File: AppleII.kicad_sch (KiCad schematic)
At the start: 0 parts

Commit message: finish tracing
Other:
- sheet Address Decoder and Onboard IO ports: added KBD_Data[0..6]; removed none
- sheet CPU Tranceiver Driver and Data MUX ports: added KBD_Data[0..6]; removed none
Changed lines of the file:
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@@
   (junction (at 140.97 101.6) (diameter 0) (color 0 0 0 0)
+  )
+  (bus (pts (xy 74.93 38.1) (xy 74.93 76.2))
+    (stroke (width 0) (type default))
   )
   (bus (pts (xy 148.59 58.42) (xy 148.59 109.22))
@@
       (effects (font (size 1.27 1.27)) (justify left))
     )
+    (pin "KBD_Data[0..6]" input (at 74.93 38.1 270)
+      (effects (font (size 1.27 1.27)) (justify left))
+    )
     (instances
       (project "AppleII"
@@
       (effects (font (size 1.27 1.27)) (justify right))
     )
+    (pin "KBD_Data[0..6]" output (at 74.93 76.2 90)
+      (effects (font (size 1.27 1.27)) (justify right))
+    )

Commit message: complete beautification
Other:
- added sheet Mounting (mounting.kicad_sch)
- added sheet Prototyping (proto.kicad_sch)
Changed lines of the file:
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@@
+    )
+  )
+  (sheet (at 60.198 154.686) (size 29.464 24.892) (fields_autoplaced)
+    (stroke (width 0.1524) (type solid))
+    (fill (color 0 0 0 0.0000))
+    (property "Sheetname" "Mounting" (at 60.198 153.9744 0)
+      (effects (font (size 1.27 1.27)) (justify left bottom))
+    )
+    (property "Sheetfile" "mounting.kicad_sch" (at 60.198 180.1626 0)
+      (effects (font (size 1.27 1.27)) (justify left top))
+    )
+    (instances
+      (project "AppleII"
+        (path "/f1f08369-4db3-46f7-9b89-a5d3cfbed55a" (page "11"))
+      )
+    )
+  )
+  (sheet (at 26.162 154.432) (size 29.718 25.146) (fields_autoplaced)
+    (stroke (width 0.1524) (type solid))
+    (fill (color 0 0 0 0.0000))
+    (property "Sheetname" "Prototyping" (at 26.162 153.7204 0)
+      (effects (font (size 1.27 1.27)) (justify left bottom))
+    )
+    (property "Sheetfile" "proto.kicad_sch" (at 26.162 180.1626 0)
+      (effects (font (size 1.27 1.27)) (justify left top))
+    )
+    (instances
+      (project "AppleII"
+        (path "/f1f08369-4db3-46f7-9b89-a5d3cfbed55a" (page "10"))
+      )
     )
   )

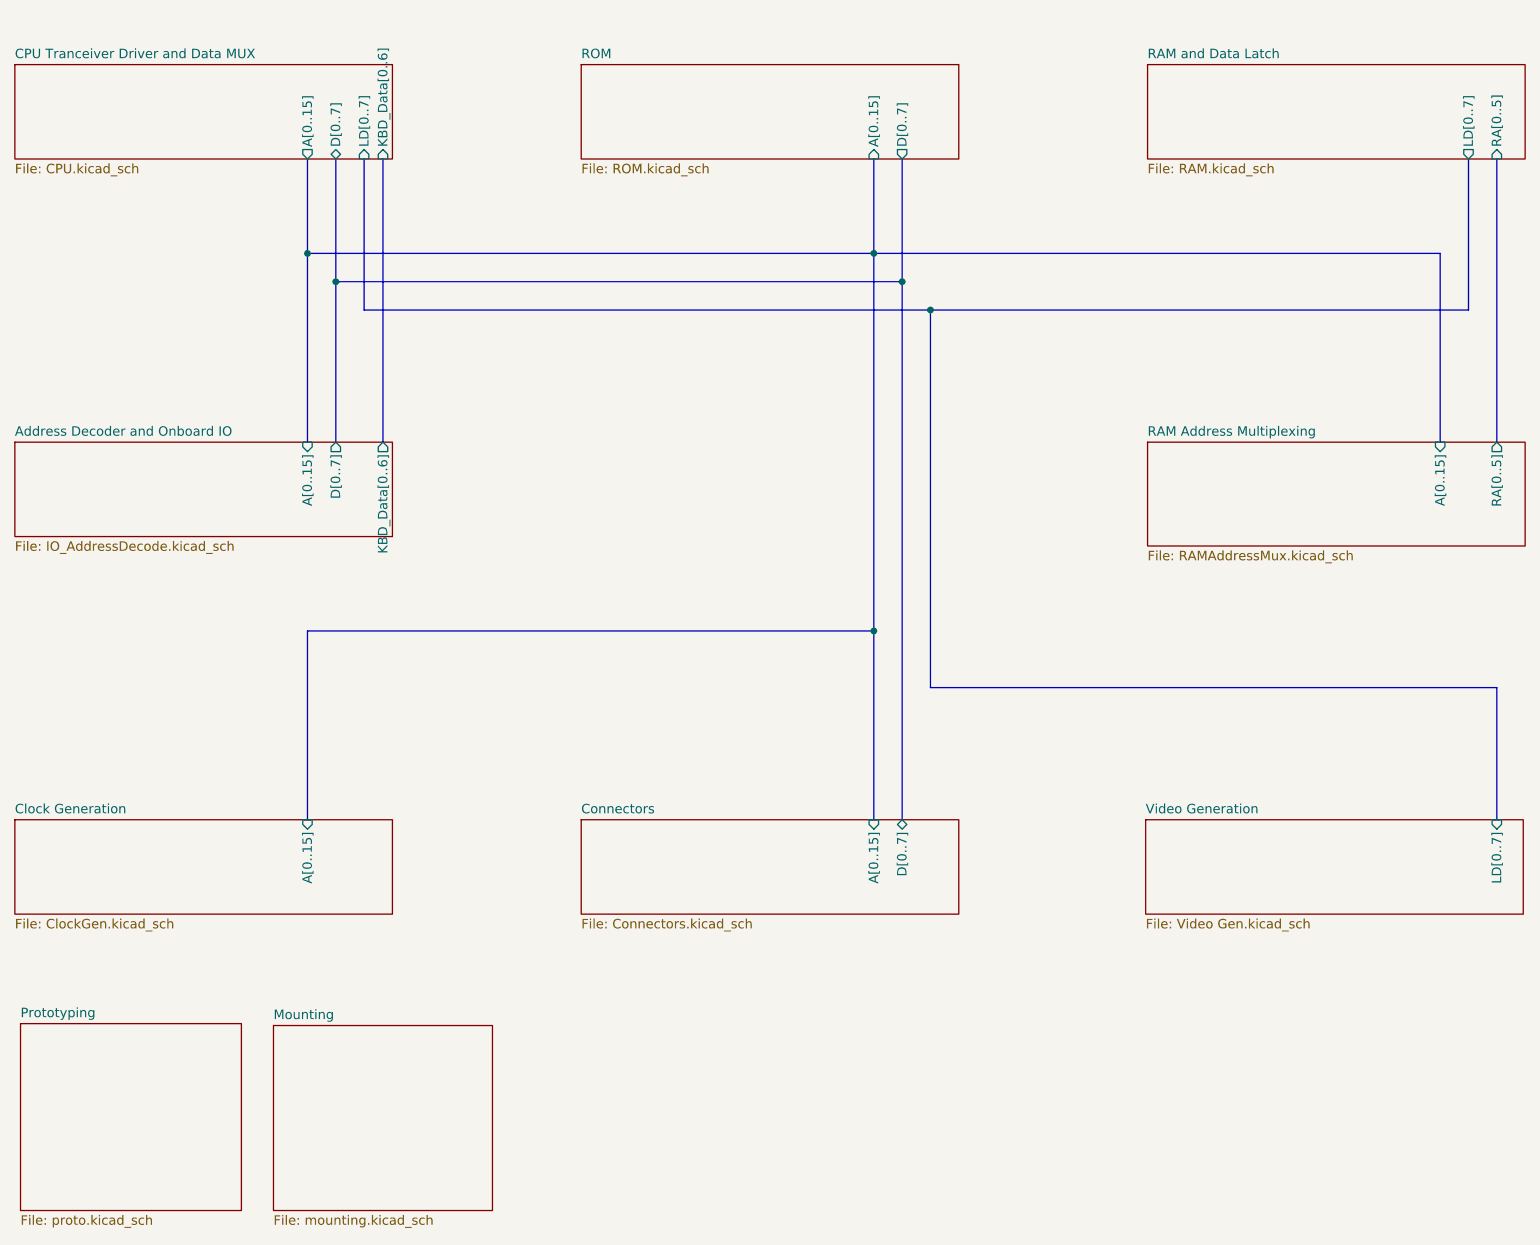
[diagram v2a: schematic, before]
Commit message: add missing test points
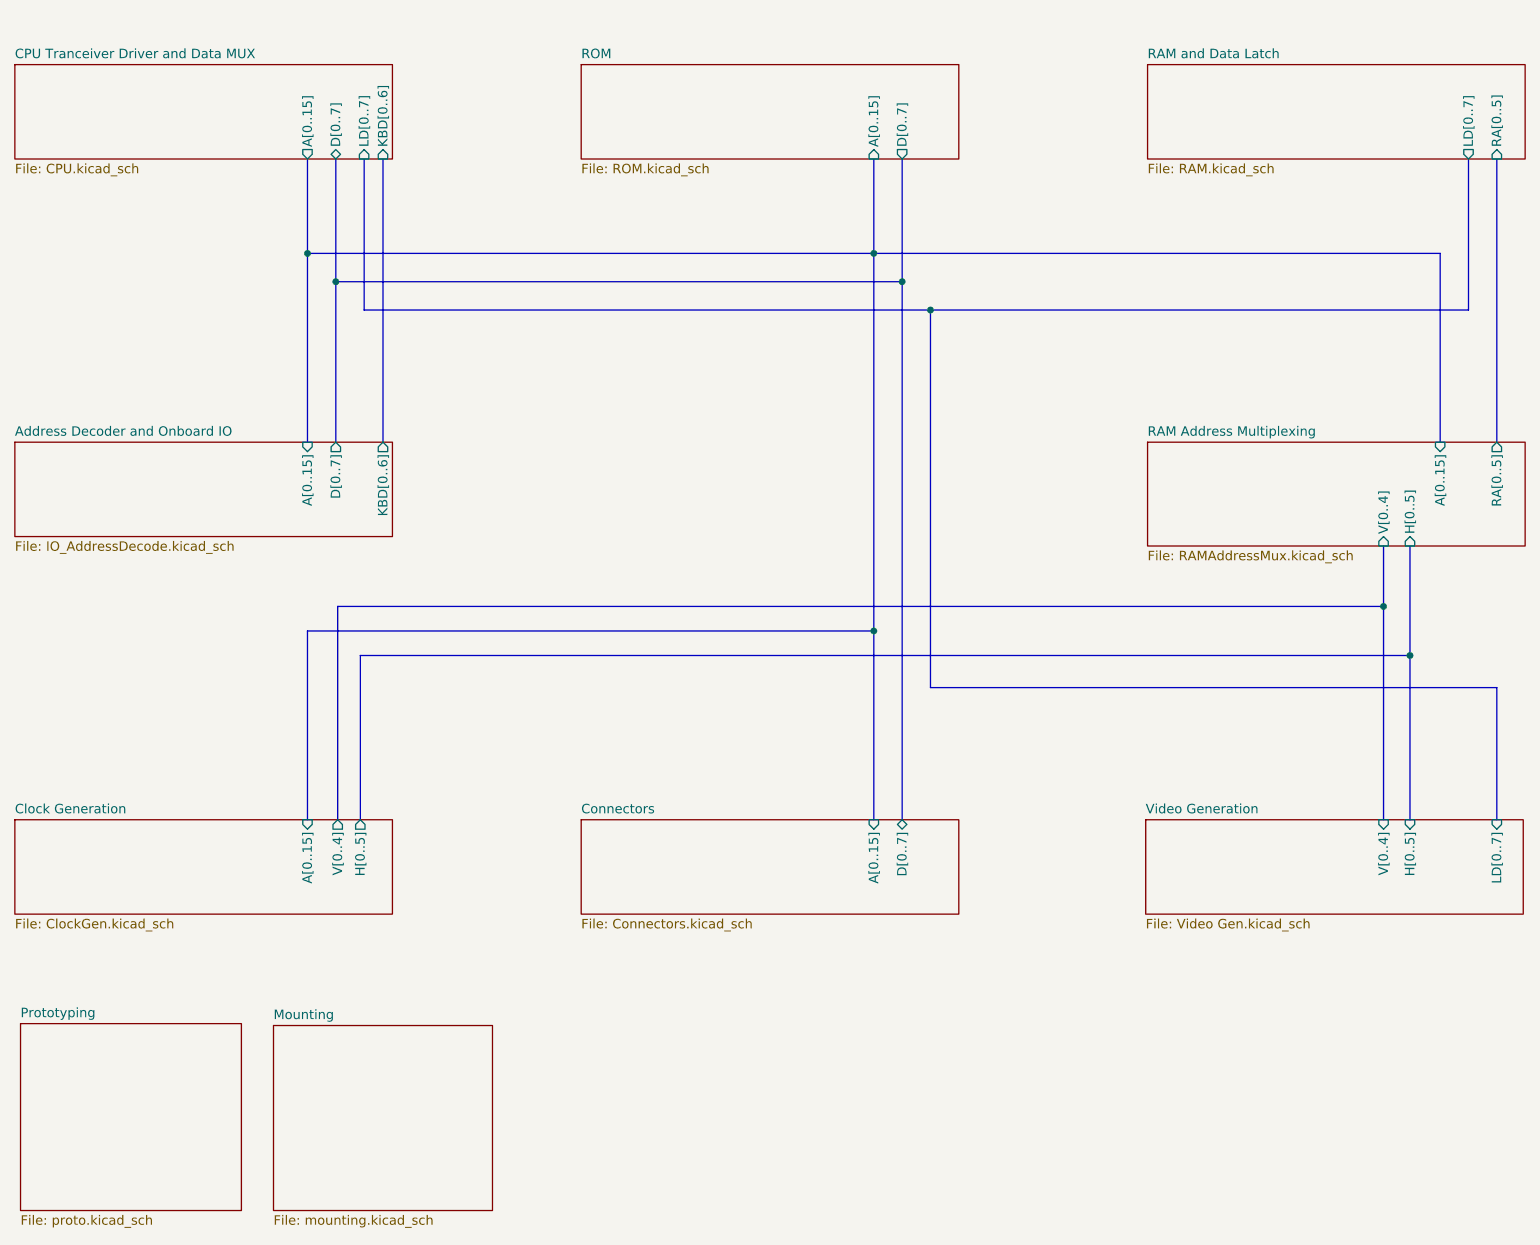
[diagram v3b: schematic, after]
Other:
- sheet Address Decoder and Onboard IO ports: added KBD[0..6]; removed KBD_Data[0..6]
- sheet CPU Tranceiver Driver and Data MUX ports: added KBD[0..6]; removed KBD_Data[0..6]
- sheet Clock Generation ports: added H[0..5], V[0..4]; removed none
- sheet RAM Address Multiplexing ports: added H[0..5], V[0..4]; removed none
- sheet Video Generation ports: added H[0..5], V[0..4]; removed none
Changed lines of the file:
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@@
   (junction (at 144.78 54.61) (diameter 0) (color 0 0 0 0)
   )
+  (junction (at 213.106 104.902) (diameter 0) (color 0 0 0 0)
+  )
   (junction (at 68.58 54.61) (diameter 0) (color 0 0 0 0)
   )
   (junction (at 64.77 50.8) (diameter 0) (color 0 0 0 0)
   )
+  (junction (at 209.55 98.298) (diameter 0) (color 0 0 0 0)
+  )
   (junction (at 140.97 50.8) (diameter 0) (color 0 0 0 0)
   )
@@
     (stroke (width 0) (type default))
   )
+  (bus (pts (xy 71.882 104.902) (xy 213.106 104.902))
+    (stroke (width 0) (type default))
+  )
   (bus (pts (xy 148.59 58.42) (xy 148.59 109.22))
     (stroke (width 0) (type default))
@@
     (stroke (width 0) (type default))
   )
+  (bus (pts (xy 209.55 90.17) (xy 209.55 98.298))
+    (stroke (width 0) (type default))
+  )
   (bus (pts (xy 140.97 50.8) (xy 140.97 101.6))
     (stroke (width 0) (type default))
   )
+  (bus (pts (xy 68.834 98.298) (xy 209.55 98.298))
+    (stroke (width 0) (type default))
+  )
   (bus (pts (xy 140.97 101.6) (xy 140.97 127))
     (stroke (width 0) (type default))
   )
+  (bus (pts (xy 68.834 127) (xy 68.834 98.298))
+    (stroke (width 0) (type default))
+  )
   (bus (pts (xy 72.39 58.42) (xy 148.59 58.42))
     (stroke (width 0) (type default))
@@
     (stroke (width 0) (type default))
   )
+  (bus (pts (xy 213.106 104.902) (xy 213.106 90.17))
+    (stroke (width 0) (type default))
+  )
   (bus (pts (xy 148.59 109.22) (xy 224.79 109.22))
     (stroke (width 0) (type default))
@@
     (stroke (width 0) (type default))
   )
+  (bus (pts (xy 71.882 127) (xy 71.882 104.902))
+    (stroke (width 0) (type default))
+  )
+  (bus (pts (xy 209.55 98.298) (xy 209.55 127))
+    (stroke (width 0) (type default))
+  )
   (bus (pts (xy 140.97 50.8) (xy 140.97 38.1))
     (stroke (width 0) (type default))
   )
+  (bus (pts (xy 213.106 104.902) (xy 213.106 127))
+    (stroke (width 0) (type default))
+  )
   (bus (pts (xy 140.97 50.8) (xy 217.17 50.8))
     (stroke (width 0) (type default))
@@
       (effects (font (size 1.27 1.27)) (justify left))
     )
-    (pin "KBD_Data[0..6]" input (at 74.93 38.1 270)
+    (pin "KBD[0..6]" input (at 74.93 38.1 270)
       (effects (font (size 1.27 1.27)) (justify left))
     )
@@
       (effects (font (size 1.27 1.27)) (justify right))
     )
+    (pin "V[0..4]" output (at 68.834 127 90)
+      (effects (font (size 1.27 1.27)) (justify right))
+    )
+    (pin "H[0..5]" output (at 71.882 127 90)
+      (effects (font (size 1.27 1.27)) (justify right))
+    )
     (instances
       (project "AppleII"
@@
       (effects (font (size 1.27 1.27)) (justify right))
     )
-    (pin "KBD_Data[0..6]" output (at 74.93 76.2 90)
+    (pin "KBD[0..6]" output (at 74.93 76.2 90)
       (effects (font (size 1.27 1.27)) (justify right))
     )
@@
       (effects (font (size 1.27 1.27)) (justify right))
     )
+    (pin "V[0..4]" input (at 209.55 90.17 270)
+      (effects (font (size 1.27 1.27)) (justify left))
+    )
+    (pin "H[0..5]" input (at 213.106 90.17 270)
+      (effects (font (size 1.27 1.27)) (justify left))
+    )
     (instances
       (project "AppleII"
@@
       (effects (font (size 1.27 1.27)) (justify right))
     )
+    (pin "H[0..5]" input (at 213.106 127 90)
+      (effects (font (size 1.27 1.27)) (justify right))
+    )
+    (pin "V[0..4]" input (at 209.55 127 90)
+      (effects (font (size 1.27 1.27)) (justify right))
+    )

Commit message: add alternative char gen footprint
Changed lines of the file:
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@@
       (effects (font (size 1.27 1.27)) (justify left))
     )
-    (pin "LD[0..7]" input (at 72.39 38.1 270)
+    (pin "LD[0..7]" bidirectional (at 72.39 38.1 270)
       (effects (font (size 1.27 1.27)) (justify left))
     )
@@
       (effects (font (size 1.27 1.27)) (justify left top))
     )
-    (pin "LD[0..7]" output (at 220.98 38.1 270)
+    (pin "LD[0..7]" bidirectional (at 220.98 38.1 270)
       (effects (font (size 1.27 1.27)) (justify left))
     )
@@
       (effects (font (size 1.27 1.27)) (justify left top))
     )
-    (pin "LD[0..7]" input (at 224.79 127 90)
+    (pin "LD[0..7]" bidirectional (at 224.79 127 90)
       (effects (font (size 1.27 1.27)) (justify right))
     )
